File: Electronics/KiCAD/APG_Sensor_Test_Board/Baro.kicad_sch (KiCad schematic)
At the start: 5 parts, among them U4 MS5607-02BA

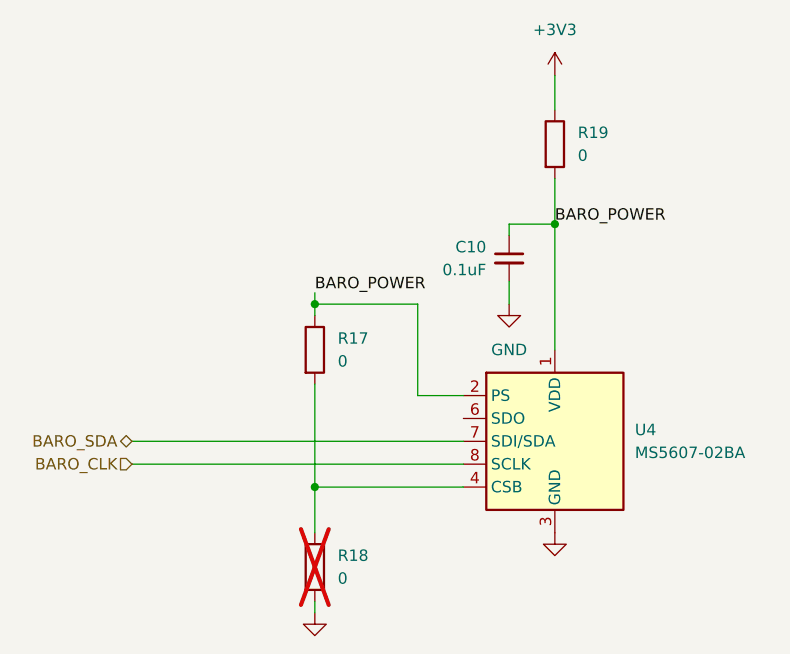
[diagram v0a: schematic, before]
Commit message: Edit PCB and Update component values
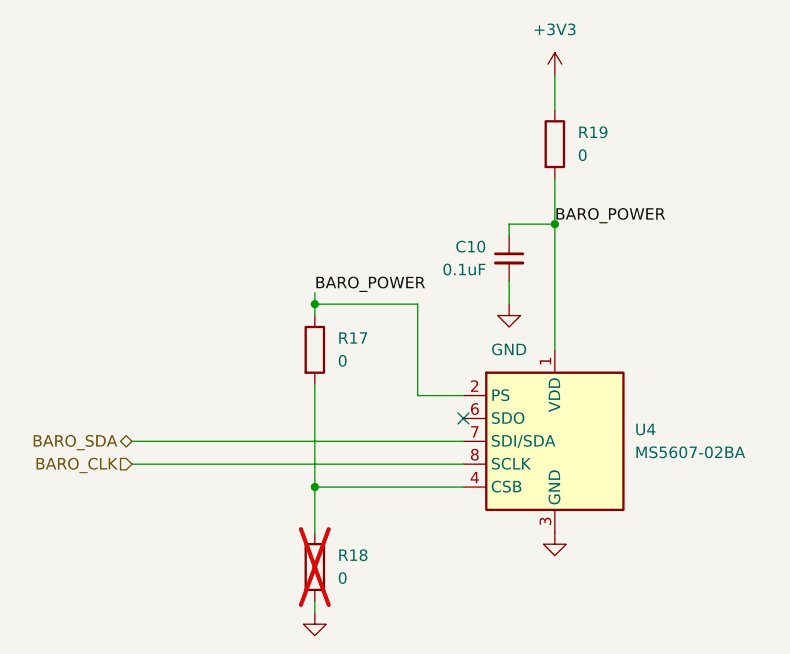
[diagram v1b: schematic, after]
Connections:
- no-connect marks 0 -> 1
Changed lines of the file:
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@@
 		(color 0 0 0 0)
+	)
+	(no_connect
+		(at 96.52 76.2)
 	)
 	(wire
